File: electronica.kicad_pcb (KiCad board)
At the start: 2 copper layers, 150 x 72 mm, 78 parts, among them J1 Conn_01x08, P12 Conn_01x03_Socket, P13 Conn_01x03_Socket, P14 Conn_01x03_Socket, P27 Conn_01x03_Socket, U1 ESP32-DevKitC, U4 ULN2003AID, U6 TSR_1-2433

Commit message: feat: final quick fixes
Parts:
- moved CP5 0.76 mm to (55.0, 102.8)
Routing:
- net IO21: track 79.1 -> 80.1 mm
- net IO33: track 93.2 -> 92.6 mm
- net 12V: track 364.5 -> 363.9 mm

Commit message: tarjeta para raspberri, pdfs y relacion de pines
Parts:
- removed G***: LOGO, LOGO
- removed RELAY1, RELAY2, RELAY3, RELAY4: SRD-12VDC-SL-C, Rele_ES32_board:RELAY_SRD-12VDC-SL-C
- removed U1: ESP32-DevKitC, PCM_Espressif:ESP32-DevKitC
- removed U2: ~, bioreactor_various:Level_Shifter_Bidir
- removed U4: ULN2003AID, ULN2003AID:SOIC127P600X175-16N
- removed UP7: XL1509-ADJ, ul_XL1509-ADJ:SOIC-8_YTS
- removed UR2, UR3: MAX3485, MAX3485:SOP8
- added J2: Raspberry_Pi_4, raspberry4-foodprint:Raspberry4-holes, F.Cu at (-62.4, 38.8)
- DP3: footprint Diode_SMD:D_SMB_Handsoldering -> Diode_THT:D_DO-41_SOD81_P10.16mm_Horizontal
- DR4, DR8: footprint Diode_SMD:D_SMA_Handsoldering -> Diode_SMD:D_SOD-323
- LP1: footprint Inductor_SMD:L_7.3x7.3_H4.5 -> Inductor_SMD:L_12x12mm_H4.5mm
- OPT1, OPT2, OPT3, OPT4: footprint Package_DIP:SMDIP-4_W9.53mm -> Package_DIP:DIP-4_W7.62mm
- moved P27 223.0 mm to (-41.8, 138.2), turned to 0 degrees
- moved P13 219.6 mm to (-41.8, 113.9), turned to 0 degrees
- moved P12 219.1 mm to (-41.8, 101.8), turned to 0 degrees
- moved P14 218.7 mm to (-41.8, 126.1), turned to 0 degrees
- moved H4 186.3 mm to (19.7, 62.1)
- moved RA3 172.5 mm to (-25.6, 112.5)
- moved CH4 172.1 mm to (-25.3, 107.5), turned to 0 degrees
- moved H2 169.8 mm to (19.7, 49.0)
- moved CH3 168.3 mm to (-25.3, 104.1), turned to 0 degrees
- moved RA4 165.6 mm to (-20.1, 112.5), turned to 0 degrees
- moved CH2 164.6 mm to (-25.3, 100.7), turned to 0 degrees
- moved CH1 161.0 mm to (-25.3, 97.3), turned to 0 degrees
- moved GTW1 146.1 mm to (-5.00, 122.1)
- moved DR7 141.3 mm to (-11.3, 120.6), turned to 0 degrees
- moved DR5 139.5 mm to (-11.3, 111.5)
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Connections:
- AN34 pad 2: 3V3 -> /IO/3V3
- AN35 pad 2: 3V3 -> /IO/3V3
- CP5 pad 1: 12V -> /power/12V
- CP6 pad 1: 12V -> /power/12V
- DP3 pad 1: 12V -> /power/12V
- PR2 pad 1: 12V -> /rs485/12V
- PR3 pad 1: 12V -> /rs485/12V
- RTC1 pad 5: 5V -> (no net)
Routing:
- net 12V: track 363.9 -> 0.00 mm, vias 3 -> 0
- net 5V: track 254.8 -> 0.00 mm, vias 5 -> 0
- net IO16: track 182.5 -> 0.00 mm, vias 1 -> 0
- net IO17: track 164.3 -> 0.00 mm, vias 4 -> 0
- net 3V3: track 157.1 -> 0.00 mm, vias 3 -> 0
- net IO33: track 92.6 -> 0.00 mm, vias 1 -> 0
- net /rs485/B1-: track 89.2 -> 0.00 mm, vias 1 -> 0
- net /rs485/A1+: track 85.2 -> 0.00 mm, vias 3 -> 0
- net /rs485/B2-: track 81.3 -> 0.00 mm, vias 3 -> 0
- net IO21: track 80.1 -> 0.00 mm, vias 1 -> 0
- net IO32: track 79.0 -> 0.00 mm, vias 3 -> 0
- net OUT1: track 75.0 -> 0.00 mm, vias 1 -> 0
- net IO36: track 74.3 -> 0.00 mm, vias 5 -> 0
- net IO13: track 69.9 -> 0.00 mm, vias 1 -> 0
- net IO0: track 68.1 -> 0.00 mm, vias 1 -> 0
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- removed copper zone on B.Cu, net GND
- removed copper zone on F.Cu, net GND
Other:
- board size 150 x 72 mm -> 115.5 x 66 mm
- board text removed: "*"
- board text removed: "+"
- board text removed: "12V"
- board text removed: "2025 · BIOR-01C · v1.0"
- board text removed: "21H"
- board text removed: "21L"
- board text removed: "23H"
- board text removed: "23L"
- board text removed: "3V"
- board text removed: "3V3"
- board text removed: "5V"
- board text removed: "A1+"
- board text removed: "A2+"
- board text removed: "B1+"
- board text removed: "B2+"
- board text removed: "GND"
- board text removed: "GND IN1"
- board text removed: "GND IN2"
- board text removed: "GND IN3"
- board text removed: "GPIO14/MTMS"
- board text removed: "IO0"
- board text removed: "IO32"
- board text removed: "IO33"
- board text removed: "IO34"
- board text removed: "LCD"
- board text removed: "Precisón Agrícola Bioreactores IOT"
- board text removed: "RTC"
- board text removed: "RX - RO"
- board text removed: "Rx"
- board text removed: "SCL"
- board text removed: "SDA"
- board text removed: "TX - DI"
- board text removed: "Tx"

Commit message: 0
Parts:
- added Bomba1: Conn_01x03_Socket, Connector_PinHeader_2.54mm:PinHeader_1x03_P2.54mm_Vertical, F.Cu at (77.9, 143.4)
- added CH5: LED, LED_SMD:LED_1206_3216Metric_Pad1.42x1.75mm_HandSolder, F.Cu at (89.5, 152.5)
- added ON/OFF1: Conn_01x03_Socket, Connector_PinHeader_2.54mm:PinHeader_1x03_P2.54mm_Vertical, F.Cu at (82.5, 143.4)
- added PWM1: Conn_01x03_Socket, Connector_PinHeader_2.54mm:PinHeader_1x03_P2.54mm_Vertical, F.Cu at (87.0, 143.4)
- added RA1: 470R, Resistor_SMD:R_Array_Convex_4x1206, F.Cu at (78.3, 154.2)
- added RA2: 330, Resistor_SMD:R_Array_Convex_4x1206, F.Cu at (83.8, 154.2)
- RA3: value 10K -> 330
- moved J1 20.6 mm to (49.0, 82.0)
- renumbered IN2 to IN1, IN4 to IN2, IN1 to IN3, IN3 to IN4
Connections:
- net 12V renamed /output/5Vin
- net IO13 renamed /output/IO16
- net IO14 renamed /output/IO24
- net IO27 renamed /output/IO23
- IN1 pad 1: IO18 -> /input/IO18
- J2 pad 1: Net-(J2-3V3-Pad1) -> 3V3
- J2 pad 12: unconnected-(J2-GPIO18/SPI1_~{CE0}/PCM_CLK/PWM0-Pad12) -> IO12
- J2 pad 16: unconnected-(J2-GPIO23/SDIO_CMD-Pad16) -> IO16
- J2 pad 17: Net-(J2-3V3-Pad1) -> 3V3
- J2 pad 18: unconnected-(J2-GPIO24/SDIO_DAT0-Pad18) -> IO18
- J2 pad 2: Net-(J2-5V-Pad2) -> 5V
- J2 pad 22: unconnected-(J2-GPIO25/SDIO_DAT1-Pad22) -> IO22
- J2 pad 36: unconnected-(J2-GPIO16/SPI1_~{CE2}-Pad36) -> IO36
- J2 pad 4: Net-(J2-5V-Pad2) -> 5V
- OPT2 pad 4: IO18 -> /input/IO18
- RA4 pad 7: IO12 -> /output/IO25

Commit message: tarjeta terminada para revisión
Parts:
- removed AN0, AN32, AN33, UARTRX2, UARTTX2: Conn_01x03_Socket, Connector_PinHeader_2.54mm:PinHeader_1x03_P2.54mm_Vertical
- removed AN34, AN35, P12, P13, P14, P27: Conn_01x03_Socket, TerminalBlock_Phoenix:TerminalBlock_Phoenix_MKDS-1,5-3_1x03_P5.00mm_Horizontal
- removed CP5, CP7: 220uF, Capacitor_THT:CP_Radial_D8.0mm_P3.50mm
- removed CP6, CP8: 0.1uF, Capacitor_SMD:C_1206_3216Metric
- removed DP3: 1N4007, Diode_THT:D_DO-41_SOD81_P10.16mm_Horizontal
- removed DR1, DR2, DR5, DR6: SMAJ6.5CA, Diode_SMD:D_SMA
- removed DR3, DR7: SMAJ12CA, Diode_SMD:D_SMA
- removed DR4, DR8: 1N5819WS, Diode_SMD:D_SOD-323
- removed GTW1: Conn_01x04, Connector_PinHeader_2.54mm:PinHeader_1x04_P2.54mm_Vertical
- removed H1, H2, H3, H4: MountingHole_Pad, MountingHole:MountingHole_2.5mm_Pad
- removed I2C4, IO15, IO2, IO22, IO4, PP18: Conn_01x02_Socket, TerminalBlock_Phoenix:TerminalBlock_Phoenix_MKDS-1,5-2_1x02_P5.00mm_Horizontal
- removed LCD-SHT1: Conn_01x04_Socket, Connector_PinHeader_2.54mm:PinHeader_1x04_P2.54mm_Vertical
- removed LP1: 68uF, Inductor_SMD:L_12x12mm_H4.5mm
- removed PR2, PR3: Conn_01x04, TerminalBlock_Phoenix:TerminalBlock_Phoenix_MKDS-1,5-4_1x04_P5.00mm_Horizontal
- removed PWR1: LED, LED_SMD:LED_1206_3216Metric_Pad1.42x1.75mm_HandSolder
- removed RN1, RN2: R_Pack04, Resistor_SMD:R_Array_Convex_4x1206
- removed RP4, RR2, RR3, RR5, RR6: 4.7k, Resistor_SMD:R_1206_3216Metric_Pad1.30x1.75mm_HandSolder
- removed RR1, RR4: 499, Resistor_SMD:R_1206_3216Metric_Pad1.30x1.75mm_HandSolder
- removed RTC1: Conn_01x04_Socket, Connector_PinHeader_2.54mm:PinHeader_1x05_P2.54mm_Vertical
- removed SDP1: SS34, Diode_SMD:D_SMA
- removed U6: TSR_1-2433, Converter_DCDC:Converter_DCDC_TRACO_TSR-1_THT
- added AN1: Conn_01x03_Socket, Connector_PinHeader_2.54mm:PinHeader_1x03_P2.54mm_Vertical, F.Cu at (84.4, 141.2)
- added AN2: Conn_01x03_Socket, Connector_PinHeader_2.54mm:PinHeader_1x03_P2.54mm_Vertical, F.Cu at (94.6, 141.2)
- added AN3: Conn_01x03_Socket, Connector_PinHeader_2.54mm:PinHeader_1x03_P2.54mm_Vertical, F.Cu at (104.8, 141.2)
- added AN4: Conn_01x03_Socket, Connector_PinHeader_2.54mm:PinHeader_1x03_P2.54mm_Vertical, F.Cu at (114.9, 141.2)
- added CP1: 220uF, Capacitor_THT:CP_Radial_D8.0mm_P3.50mm, F.Cu at (124.5, 81.0)
- added CP2: 0.1uF, Capacitor_SMD:C_1206_3216Metric, F.Cu at (136.5, 89.0)
- added CP3: 220uF, Capacitor_THT:CP_Radial_D8.0mm_P3.50mm, F.Cu at (133.5, 81.0)
- added CP4: 0.1uF, Capacitor_SMD:C_1206_3216Metric, F.Cu at (131.2, 89.0)
- added D1: D-SR5100, Diode_THT:D_DO-41_SOD81_P7.62mm_Horizontal, F.Cu at (129.9, 63.5)
- added F1: 3A, Fuse:Fuse_0603_1608Metric, F.Cu at (124.7, 138.5)
- added F3: 5A, Fuse:Fuse_1206_3216Metric, F.Cu at (136.0, 73.0)
- added F4: 3A, Fuse:Fuse_0603_1608Metric, F.Cu at (136.1, 102.2)
- added J3: Conn_01x12, Connector_Samtec_HPM_THT:Samtec_HPM-12-05-x-S_Straight_1x12_Pitch5.08mm, F.Cu at (45.6, 141.5)
- added J4: Conn_01x05, Connector_PinHeader_2.00mm:PinHeader_1x05_P2.00mm_Vertical, F.Cu at (102.5, 103.2)
- added P1: Conn_01x03_Socket, TerminalBlock_Phoenix:TerminalBlock_Phoenix_MKDS-1,5-3_1x03_P5.00mm_Horizontal, F.Cu at (55.0, 54.3)
- added P2: Conn_01x03_Socket, TerminalBlock_Phoenix:TerminalBlock_Phoenix_MKDS-1,5-3_1x03_P5.00mm_Horizontal, F.Cu at (71.0, 54.3)
- added P3: Conn_01x03_Socket, TerminalBlock_Phoenix:TerminalBlock_Phoenix_MKDS-1,5-3_1x03_P5.00mm_Horizontal, F.Cu at (88.5, 54.3)
- added P4: Conn_01x03_Socket, TerminalBlock_Phoenix:TerminalBlock_Phoenix_MKDS-1,5-3_1x03_P5.00mm_Horizontal, F.Cu at (105.5, 54.3)
- added PP1: Conn_01x02_Socket, TerminalBlock_Phoenix:TerminalBlock_Phoenix_MKDS-1,5-2_1x02_P5.00mm_Horizontal, F.Cu at (131.5, 55.5)
- added PWR-IN1: LED, LED_SMD:LED_1206_3216Metric_Pad1.42x1.75mm_HandSolder, F.Cu at (136.0, 68.5)
- added PWR-OP1: LED, LED_SMD:LED_1206_3216Metric_Pad1.42x1.75mm_HandSolder, F.Cu at (129.0, 108.2)
- added RELAY1: SRD-05DC-SL-C, Relay_THT:Relay_SPDT_Finder_36.11, F.Cu at (56.0, 76.5)
- added RELAY2: SRD-05DC-SL-C, Relay_THT:Relay_SPDT_Finder_36.11, F.Cu at (72.8, 76.5)
- added RELAY3: SRD-05DC-SL-C, Relay_THT:Relay_SPDT_Finder_36.11, F.Cu at (89.7, 76.5)
- added RELAY4: SRD-05DC-SL-C, Relay_THT:Relay_SPDT_Finder_36.11, F.Cu at (106.5, 76.5)
- added RN1-1: 1k, Resistor_SMD:R_Array_Convex_4x1206, F.Cu at (65.5, 86.3)
- added RN2-1: 330, Resistor_SMD:R_Array_Convex_4x1206, F.Cu at (54.2, 134.5)
- added RP1: 330, Resistor_SMD:R_1206_3216Metric_Pad1.30x1.75mm_HandSolder, F.Cu at (130.4, 68.5)
- added RP2: 330, Resistor_SMD:R_1206_3216Metric_Pad1.30x1.75mm_HandSolder, F.Cu at (129.0, 104.2)
- added RPwr1: 500, Resistor_SMD:R_1206_3216Metric_Pad1.30x1.75mm_HandSolder, F.Cu at (126.0, 89.0)
- added U1: ADS1115 MOD, Connector_PinHeader_2.54mm:ADS1115, F.Cu at (95.2, 124.7)
- added U2: ULN2003AID, Package_SO:SOIC-16W_5.3x10.2mm_P1.27mm, F.Cu at (115.1, 71.2)
- added U3: ~, Connector_PinHeader_2.54mm:LVL Shifter, F.Cu at (77.2, 112.7)
- added UART1: Conn_01x05, Connector_PinHeader_2.00mm:PinHeader_1x05_P2.00mm_Vertical, F.Cu at (77.0, 87.5)
- J1: value Conn_01x08 -> Conn_02x02_Counter_Clockwise; footprint TerminalBlock_Phoenix:TerminalBlock_Phoenix_MKDS-1,5-8_1x08_P5.00mm_Horizontal -> Connector_PinHeader_2.54mm:PinHeader_2x02_P2.54mm_Vertical
- RA2: value 330 -> 470R
- RA4: value 470R -> 330
- moved J2 175.7 mm to (104.0, 95.0)
- moved CH4 157.5 mm to (123.0, 54.5), turned to 90 degrees
- moved CH3 153.0 mm to (119.5, 54.5), turned to 90 degrees
- moved RA4 150.9 mm to (122.0, 61.8)
- moved RA3 149.9 mm to (115.5, 61.8)
- moved CH2 148.6 mm to (116.0, 54.5), turned to 90 degrees
- moved CH1 144.3 mm to (112.5, 54.5), turned to 90 degrees
- moved CH5 104.8 mm to (126.5, 54.5), turned to 90 degrees
- moved RA2 75.8 mm to (116.6, 85.9), turned to -90 degrees
- moved RA1 75.4 mm to (110.4, 85.9), turned to -90 degrees
- moved Bomba1 61.9 mm to (56.0, 85.5)
- moved ON/OFF1 55.1 mm to (130.0, 115.6)
- moved IN3 55.0 mm to (60.4, 142.0), turned to 90 degrees
- moved IN4 50.9 mm to (64.6, 142.0), turned to 90 degrees
- moved IN1 49.0 mm to (52.0, 142.0), turned to 90 degrees
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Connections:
- net /output/IO38 renamed IO38
- net 3V3 renamed /3V3
- Bomba1 pad 2: /output/5Vin -> /5V
- IN1 pad 1: /input/IO18 -> IO04
- IN2 pad 1: IO25 -> IO17
- IN3 pad 1: IO19 -> IO27
- IN4 pad 1: IO5 -> IO22
- J1 pad 1: GND -> IO03-SCL
- J1 pad 2: IN1 -> Net-(J1-Pin_1)
- J1 pad 3: GND -> IO02-SDA
- J1 pad 4: IN2 -> Net-(J1-Pin_2)
- J2 pad 10: unconnected-(J2-GPIO15/UART_RXD-Pad10) -> Net-(J2-GPIO15/UART_RXD)
- J2 pad 11: unconnected-(J2-GPIO17/SPI1_~{CE1}-Pad11) -> IO17
- J2 pad 12: IO12 -> IO18
- J2 pad 13: unconnected-(J2-GPIO27/SDIO_DAT3-Pad13) -> IO27
- J2 pad 14: Net-(J2-GND-Pad14) -> GND
- J2 pad 15: unconnected-(J2-GPIO22/SDIO_CLK-Pad15) -> IO22
- J2 pad 16: IO16 -> IO23
- J2 pad 18: IO18 -> IO24
- J2 pad 19: unconnected-(J2-MOSI_SPI0/GPIO10-Pad19) -> MOSI
- J2 pad 2: 5V -> /5V
- J2 pad 20: Net-(J2-GND-Pad14) -> GND
- J2 pad 21: unconnected-(J2-MISO_SPI0/GPIO09-Pad21) -> MISO
- J2 pad 22: IO22 -> IO25
- J2 pad 23: unconnected-(J2-SCLK_SPI0/GPIO11-Pad23) -> Net-(J2-SCLK_SPI0/GPIO11)
- J2 pad 25: Net-(J2-GND-Pad14) -> GND
- J2 pad 29: unconnected-(J2-GPCLK1/GPIO05-Pad29) -> IO05
- J2 pad 3: unconnected-(J2-SDA_I2C1/GPIO02-Pad3) -> IO02-SDA
- J2 pad 30: Net-(J2-GND-Pad14) -> GND
- J2 pad 32: unconnected-(J2-GPIO12/PWM0-Pad32) -> IO32
- J2 pad 33: unconnected-(J2-GPIO13/PWM1-Pad33) -> ADDR
- J2 pad 34: Net-(J2-GND-Pad14) -> GND
- J2 pad 36: IO36 -> IO16
- J2 pad 39: Net-(J2-GND-Pad14) -> GND
- J2 pad 4: 5V -> /5V
- J2 pad 40: unconnected-(J2-GPIO21/SPI1_SCLK/PCM_DOUT-Pad40) -> IO21
- J2 pad 5: unconnected-(J2-SCL_I2C1/GPIO03-Pad5) -> IO03-SCL
- J2 pad 6: Net-(J2-GND-Pad14) -> GND
- J2 pad 7: unconnected-(J2-GPCLK0/GPIO04-Pad7) -> IO04
- J2 pad 8: unconnected-(J2-GPIO14/UART_TXD-Pad8) -> Net-(J2-GPIO14/UART_TXD)
- J2 pad 9: Net-(J2-GND-Pad14) -> GND
- ON/OFF1 pad 2: /output/5Vin -> /5V
- ON/OFF1 pad 3: /output/IO40 -> IO21
- OPT1 pad 1: INW1 -> Net-(RN1-1-R4.1)
- OPT1 pad 4: IO19 -> IO22
- OPT2 pad 1: INW2 -> Net-(RN1-1-R3.1)
- OPT2 pad 4: /input/IO18 -> IO27
- OPT3 pad 1: INW3 -> Net-(RN1-1-R2.1)
- OPT3 pad 4: IO5 -> IO17
- OPT4 pad 1: INW4 -> Net-(RN1-1-R1.1)
- OPT4 pad 4: IO25 -> IO04
- PWM1 pad 2: /output/5Vin -> /5V
- PWM1 pad 3: /output/IO18 -> IO32
- RA1 pad 1: unconnected-(RA1-R1.1-Pad1) -> Net-(RA1-R1.1)
- RA1 pad 5: /output/IO36 -> IO23
- RA1 pad 6: unconnected-(RA1-R3.2-Pad6) -> IO24
- RA1 pad 7: unconnected-(RA1-R2.2-Pad7) -> IO25
- RA1 pad 8: unconnected-(RA1-R1.2-Pad8) -> IO16
- RA2 pad 2: unconnected-(RA2-R2.1-Pad2) -> Net-(RA2-R2.1)
- RA2 pad 3: unconnected-(RA2-R3.1-Pad3) -> Net-(RA2-R3.1)
- RA2 pad 4: Net-(CH5-A) -> Net-(RA2-R4.1)
- RA2 pad 5: /output/5Vin -> IO18
- RA3 pad 1: Net-(CH4-A) -> Net-(CH1-A)
- RA3 pad 2: Net-(CH3-A) -> Net-(CH2-A)
- RA3 pad 3: Net-(CH2-A) -> Net-(CH3-A)
- RA3 pad 4: Net-(CH1-A) -> Net-(CH4-A)
- RA3 pad 5: /output/5Vin -> /5V
- RA3 pad 6: /output/5Vin -> /5V
- RA3 pad 7: /output/5Vin -> /5V
- RA3 pad 8: /output/5Vin -> /5V
- RA4 pad 1: Net-(RA4-R1.1) -> Net-(CH5-A)
- RA4 pad 2: Net-(RA4-R2.1) -> unconnected-(RA4-R2.1-Pad2)
- RA4 pad 3: Net-(RA4-R3.1) -> unconnected-(RA4-R3.1-Pad3)
- RA4 pad 4: Net-(RA4-R4.1) -> unconnected-(RA4-R4.1-Pad4)
- RA4 pad 5: /output/IO23 -> unconnected-(RA4-R4.2-Pad5)
- RA4 pad 6: /output/IO24 -> unconnected-(RA4-R3.2-Pad6)
- RA4 pad 7: /output/IO25 -> unconnected-(RA4-R2.2-Pad7)
- RA4 pad 8: /output/IO16 -> /5V
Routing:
- net /5V: track 0.00 -> 356.4 mm, vias 0 -> 4
- net /VIN: track 0.00 -> 204.0 mm
- net CONTROL SENORES: track 0.00 -> 132.5 mm, vias 0 -> 1
- net IO22: track 0.00 -> 82.4 mm, vias 0 -> 1
- net IO27: track 0.00 -> 76.3 mm, vias 0 -> 2
- net OUT1: track 0.00 -> 71.7 mm
- net IO17: track 0.00 -> 71.5 mm, vias 0 -> 2
- net IO32: track 0.00 -> 70.0 mm
- net IO04: track 0.00 -> 65.8 mm, vias 0 -> 2
- net OUT2: track 0.00 -> 63.0 mm
- net ADDR: track 0.00 -> 59.7 mm
- net /3V3: track 0.00 -> 51.9 mm
- net /5V-SENSE: track 0.00 -> 50.6 mm
- net Net-(RN1-1-R1.1): track 0.00 -> 45.1 mm
- net OUT3: track 0.00 -> 44.8 mm
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- added copper zone on B.Cu, net GND
- added copper zone on F.Cu, net GND
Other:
- board size 115.5 x 66 mm -> 100 x 100 mm
- board text added: "5-MOSI-MISO-NA-GND"
- board text added: "PRECISION AGRICOLA BIO-RPB1"
- board text added: "S +5V GND"

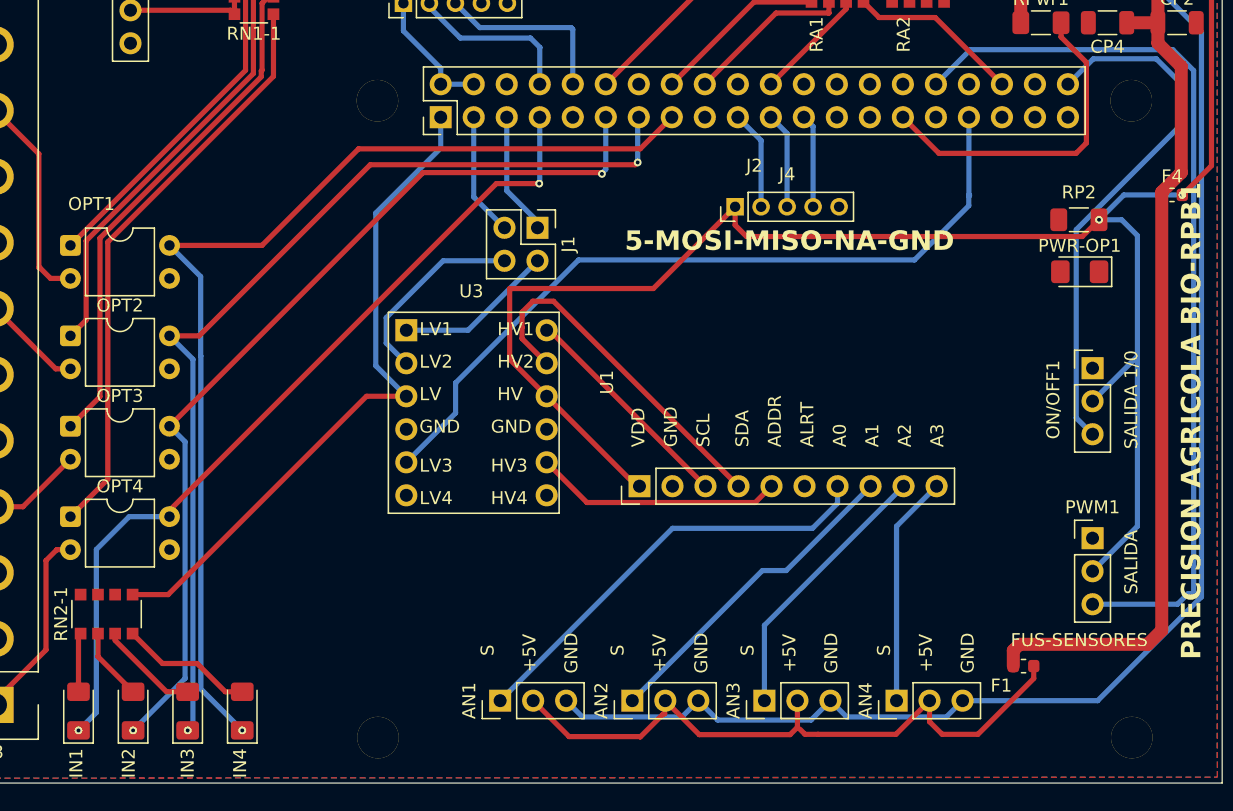
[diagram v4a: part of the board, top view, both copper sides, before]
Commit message: conecciones corregidas
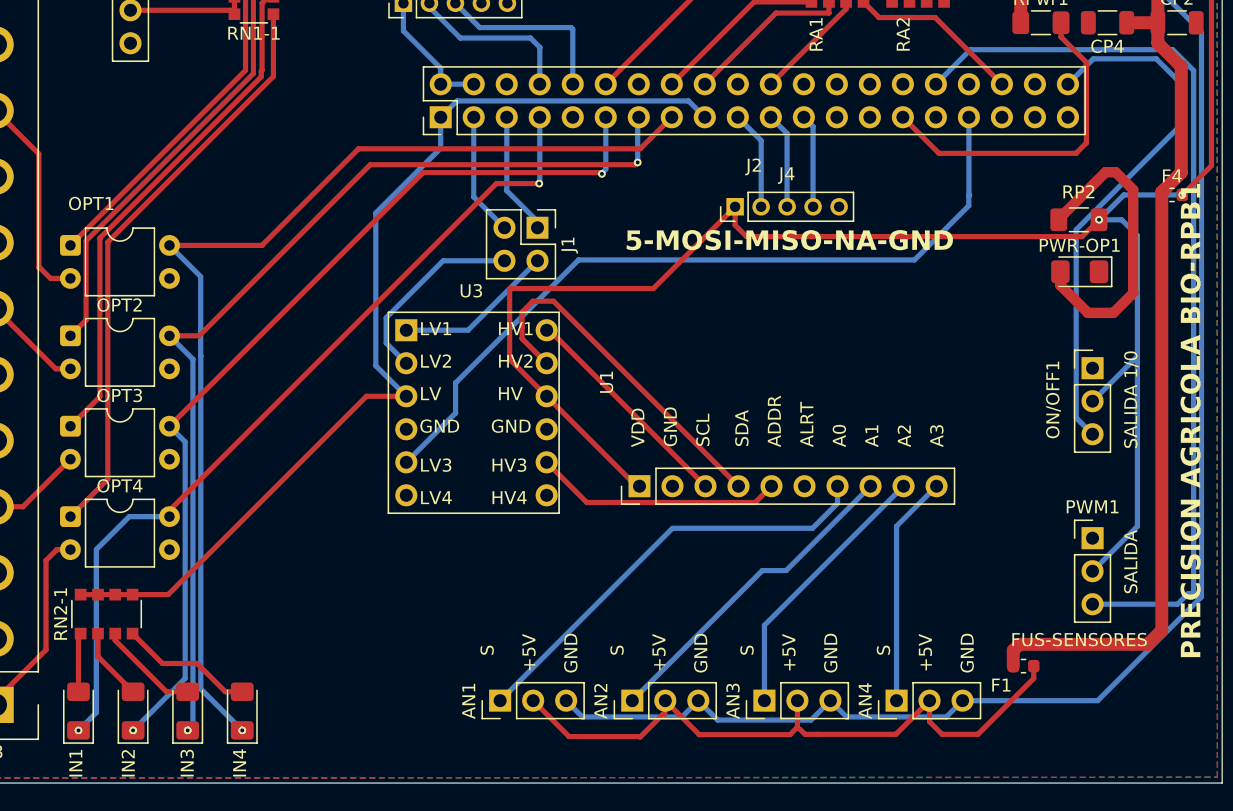
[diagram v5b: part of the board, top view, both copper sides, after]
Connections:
- J1 pad 1: IO03-SCL -> Net-(J1-Pin_1)
- J1 pad 2: Net-(J1-Pin_1) -> Net-(J1-Pin_2)
- J1 pad 4: Net-(J1-Pin_2) -> IO03-SCL
- J2 pad 40: IO21 -> unconnected-(J2-GPIO21/SPI1_SCLK/PCM_DOUT-Pad40)
- ON/OFF1 pad 3: IO21 -> IO40
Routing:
- net IO21: track 41.4 -> 0.00 mm
- net (no net): track 0.00 -> 41.4 mm
- net /3V3: track 51.9 -> 77.3 mm
- net Net-(PWR-OP1-A): track 0.00 -> 23.9 mm
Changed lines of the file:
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@@
 	(net 27 "/VIN")
 	(net 28 "unconnected-(J2-GPIO19{slash}SPI1_MISO{slash}PCM_FS-Pad35)")
-	(net 29 "IO21")
+	(net 29 "unconnected-(J2-GPIO21{slash}SPI1_SCLK{slash}PCM_DOUT-Pad40)")
 	(net 30 "Net-(D1-K)")
 	(net 31 "unconnected-(J2-GPIO20{slash}SPI1_MOSI{slash}PCM_DIN{slash}PWM1-Pad38)")
@@
 	(net 103 "MOSI")
 	(net 104 "MISO")
+	(net 105 "IO40")
 	(footprint "Diode_THT:D_DO-41_SOD81_P7.62mm_Horizontal"
 		(layer "F.Cu")
@@
 			(layers "*.Cu" "*.Mask")
 			(remove_unused_layers no)
-			(net 22 "IO03-SCL")
-			(pinfunction "Pin_4")
+			(net 97 "Net-(J1-Pin_1)")
+			(pinfunction "Pin_1")
 			(pintype "passive")
 		)
@@
 			(layers "*.Cu" "*.Mask")
 			(remove_unused_layers no)
-			(net 97 "Net-(J1-Pin_1)")
-			(pinfunction "Pin_1")
+			(net 99 "Net-(J1-Pin_2)")
+			(pinfunction "Pin_2")
 			(pintype "passive")
 		)
@@
 			(layers "*.Cu" "*.Mask")
 			(remove_unused_layers no)
-			(net 99 "Net-(J1-Pin_2)")
-			(pinfunction "Pin_2")
+			(net 22 "IO03-SCL")
+			(pinfunction "Pin_4")
 			(pintype "passive")
 		)
@@
 			(layers "*.Cu" "*.Mask")
 			(remove_unused_layers no)
-			(net 29 "IO21")
+			(net 105 "IO40")
 			(pinfunction "Pin_3")
 			(pintype "passive")
@@
 		(pad "" thru_hole circle
 			(at -29.044 0 180)
-			(size 3.2 3.2)
-			(drill 3.2)
-			(layers "*.Cu" "*.Mask")
+			(size 1 1)
+			(drill 3.5)
+			(layers "*.Cu")
 			(remove_unused_layers no)
 			(solder_mask_margin 1.625)
@@
 		(pad "" thru_hole circle
 			(at -29 49 180)
-			(size 3.2 3.2)
-			(drill 3.2)
-			(layers "*.Cu" "*.Mask")
+			(size 1 1)
+			(drill 3.5)
+			(layers "*.Cu")
 			(remove_unused_layers no)
 			(solder_mask_margin 1.625)
@@
 		(pad "" thru_hole circle
 			(at 28.956 0 180)
-			(size 3.2 3.2)
-			(drill 3.2)
-			(layers "*.Cu" "*.Mask")
+			(size 1 1)
+			(drill 3.5)
+			(layers "*.Cu")
 			(remove_unused_layers no)
 			(solder_mask_margin 1.625)
@@
 		(pad "" thru_hole circle
 			(at 29 49 180)
-			(size 3.2 3.2)
-			(drill 3.2)
-			(layers "*.Cu" "*.Mask")
+			(size 1 1)
+			(drill 3.5)
+			(layers "*.Cu")
 			(remove_unused_layers no)
 			(solder_mask_margin 1.625)
@@
 			(layers "*.Cu" "*.Mask")
 			(remove_unused_layers no)
-			(net 29 "IO21")
+			(net 29 "unconnected-(J2-GPIO21{slash}SPI1_SCLK{slash}PCM_DOUT-Pad40)")
 			(pinfunction "GPIO21/SPI1_SCLK/PCM_DOUT")
 			(pintype "bidirectional")
@@
 	)
 	(segment
+		(start 136.975 97)
+		(end 136.975 93.825)
+		(width 0.4)
+		(layer "B.Cu")
+		(net 0)
+	)
+	(segment
+		(start 130.085 91.775)
+		(end 128.13 93.73)
+		(width 0.4)
+		(layer "B.Cu")
+		(net 0)
+	)
+	(segment
+		(start 134.925 91.775)
+		(end 130.085 91.775)
+		(width 0.4)
+		(layer "B.Cu")
+		(net 0)
+	)
+	(segment
+		(start 128.7678 119.4058)
+		(end 128.7678 104.91831)
+		(width 0.4)
+		(layer "B.Cu")
+		(net 0)
+	)
+	(segment
+		(start 128.7678 104.91831)
+		(end 136.68611 97)
+		(width 0.4)
+		(layer "B.Cu")
+		(net 0)
+	)
+	(segment
+		(start 130.022 120.66)
+		(end 128.7678 119.4058)
+		(width 0.4)
+		(layer "B.Cu")
+		(net 0)
+	)
+	(segment
+		(start 136.975 93.825)
+		(end 134.925 91.775)
+		(width 0.4)
+		(layer "B.Cu")
+		(net 0)
+	)
+	(segment
+		(start 136.68611 97)
+		(end 136.975 97)
+		(width 0.4)
+		(layer "B.Cu")
+		(net 0)
+	)
+	(segment
 		(start 137.5 63.5)
 		(end 137.5 68.5)
@@
 	)
 	(segment
+		(start 54.82 133)
+		(end 52.16 133)
+		(width 0.4)
+		(layer "F.Cu")
+		(net 25)
+	)
+	(segment
 		(start 58.9 133)
 		(end 74.16 117.74)
@@
 	)
 	(segment
+		(start 54.82 133)
+		(end 56.16 133)
+		(width 0.4)
+		(layer "F.Cu")
+		(net 25)
+	)
+	(segment
 		(start 74.16 117.74)
 		(end 77.222 117.74)
@@
 	)
 	(segment
+		(start 100.19 96.27)
+		(end 98.9358 95.0158)
+		(width 0.4)
+		(layer "B.Cu")
+		(net 25)
+	)
+	(segment
+		(start 98.9358 95.0158)
+		(end 81.1242 95.0158)
+		(width 0.4)
+		(layer "B.Cu")
+		(net 25)
+	)
+	(segment
 		(start 74.875 103.64)
 		(end 79.87 98.645)
@@
 	)
 	(segment
+		(start 81.1242 95.0158)
+		(end 79.87 96.27)
+		(width 0.4)
+		(layer "B.Cu")
+		(net 25)
+	)
+	(segment
 		(start 79.87 98.645)
 		(end 79.87 96.27)
@@
 	)
 	(segment
-		(start 136.975 97)
-		(end 136.975 93.825)
-		(width 0.4)
-		(layer "B.Cu")
-		(net 29)
-	)
-	(segment
-		(start 130.085 91.775)
-		(end 128.13 93.73)
-		(width 0.4)
-		(layer "B.Cu")
-		(net 29)
-	)
-	(segment
-		(start 134.925 91.775)
-		(end 130.085 91.775)
-		(width 0.4)
-		(layer "B.Cu")
-		(net 29)
-	)
-	(segment
-		(start 128.7678 119.4058)
-		(end 128.7678 104.91831)
-		(width 0.4)
-		(layer "B.Cu")
-		(net 29)
-	)
-	(segment
-		(start 128.7678 104.91831)
-		(end 136.68611 97)
-		(width 0.4)
-		(layer "B.Cu")
-		(net 29)
-	)
-	(segment
-		(start 130.022 120.66)
-		(end 128.7678 119.4058)
-		(width 0.4)
-		(layer "B.Cu")
-		(net 29)
-	)
-	(segment
-		(start 136.975 93.825)
-		(end 134.925 91.775)
-		(width 0.4)
-		(layer "B.Cu")
-		(net 29)
-	)
-	(segment
-		(start 136.68611 97)
-		(end 136.975 97)
-		(width 0.4)
-		(layer "B.Cu")
-		(net 29)
-	)
-	(segment
 		(start 129.88 56.97)
 		(end 129.88 63.5)
@@
 		(net 71)
 	)
+	(segment
+		(start 127.422 104.16)
+		(end 127.422 104.103)
+		(width 0.8)
+		(layer "F.Cu")
+		(net 72)
+	)
+	(segment
+		(start 131.025 100.5)
+		(end 131.8 100.5)
+		(width 0.8)
+		(layer "F.Cu")
+		(net 72)
+	)
+	(segment
+		(start 131.625 111.325)
+		(end 129.675 111.325)
+		(width 0.8)
+		(layer "F.Cu")
+		(net 72)
+	)
+	(segment
+		(start 131.8 100.5)
+		(end 133.15 101.85)
+		(width 0.8)
+		(layer "F.Cu")
+		(net 72)
+	)
+	(segment
+		(start 133.15 109.8)
+		(end 131.625 111.325)
+		(width 0.8)
+		(layer "F.Cu")
+		(net 72)
+	)
+	(segment
+		(start 127.422 104.103)
+		(end 131.025 100.5)
+		(width 0.8)
+		(layer "F.Cu")
+		(net 72)
+	)
+	(segment
+		(start 127.547 109.197)
+		(end 127.547 108.16)
+		(width 0.8)
+		(layer "F.Cu")
+		(net 72)
+	)
+	(segment
+		(start 133.15 101.85)
+		(end 133.15 109.8)
+		(width 0.8)
+		(layer "F.Cu")
+		(net 72)
+	)
+	(segment
+		(start 129.675 111.325)
+		(end 127.547 109.197)
+		(width 0.8)
+		(layer "F.Cu")
+		(net 72)
+	)
 	(via
